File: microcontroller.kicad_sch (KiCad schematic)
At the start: 71 parts, among them J100 Conn_01x05_Pin, J101 Conn_01x03, J103 Screw_Terminal_01x02, J104 USB_C_Receptacle_USB2.0_16P, Q100 Si2371EDS, SW100 K2-1157SP-I4SW-04, U100 STM32H563RITx, U101 AP2112K-3.3, U102 USBLC6-2SC6, Y100 X322516MMB4SI

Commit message: Apply Daniel's suggestions
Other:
- moved on the sheet: FB100

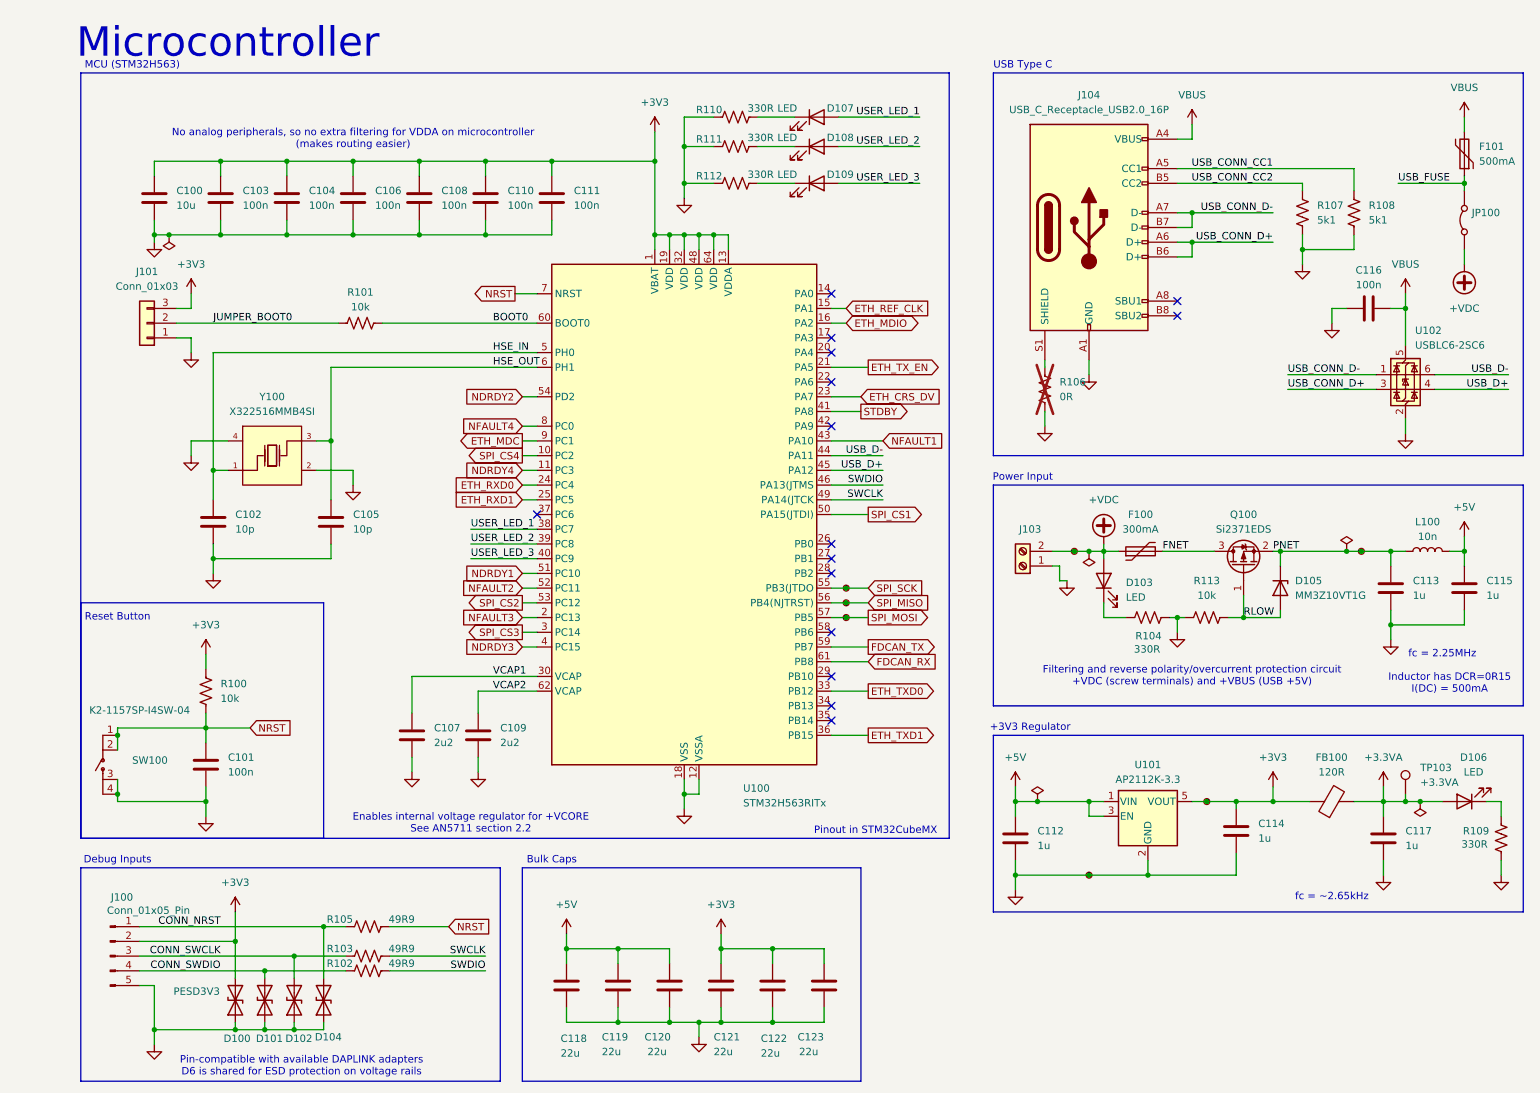
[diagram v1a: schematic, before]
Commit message: Modify repo for usage on Linux, add basic CI
chore: fix CI

Small things
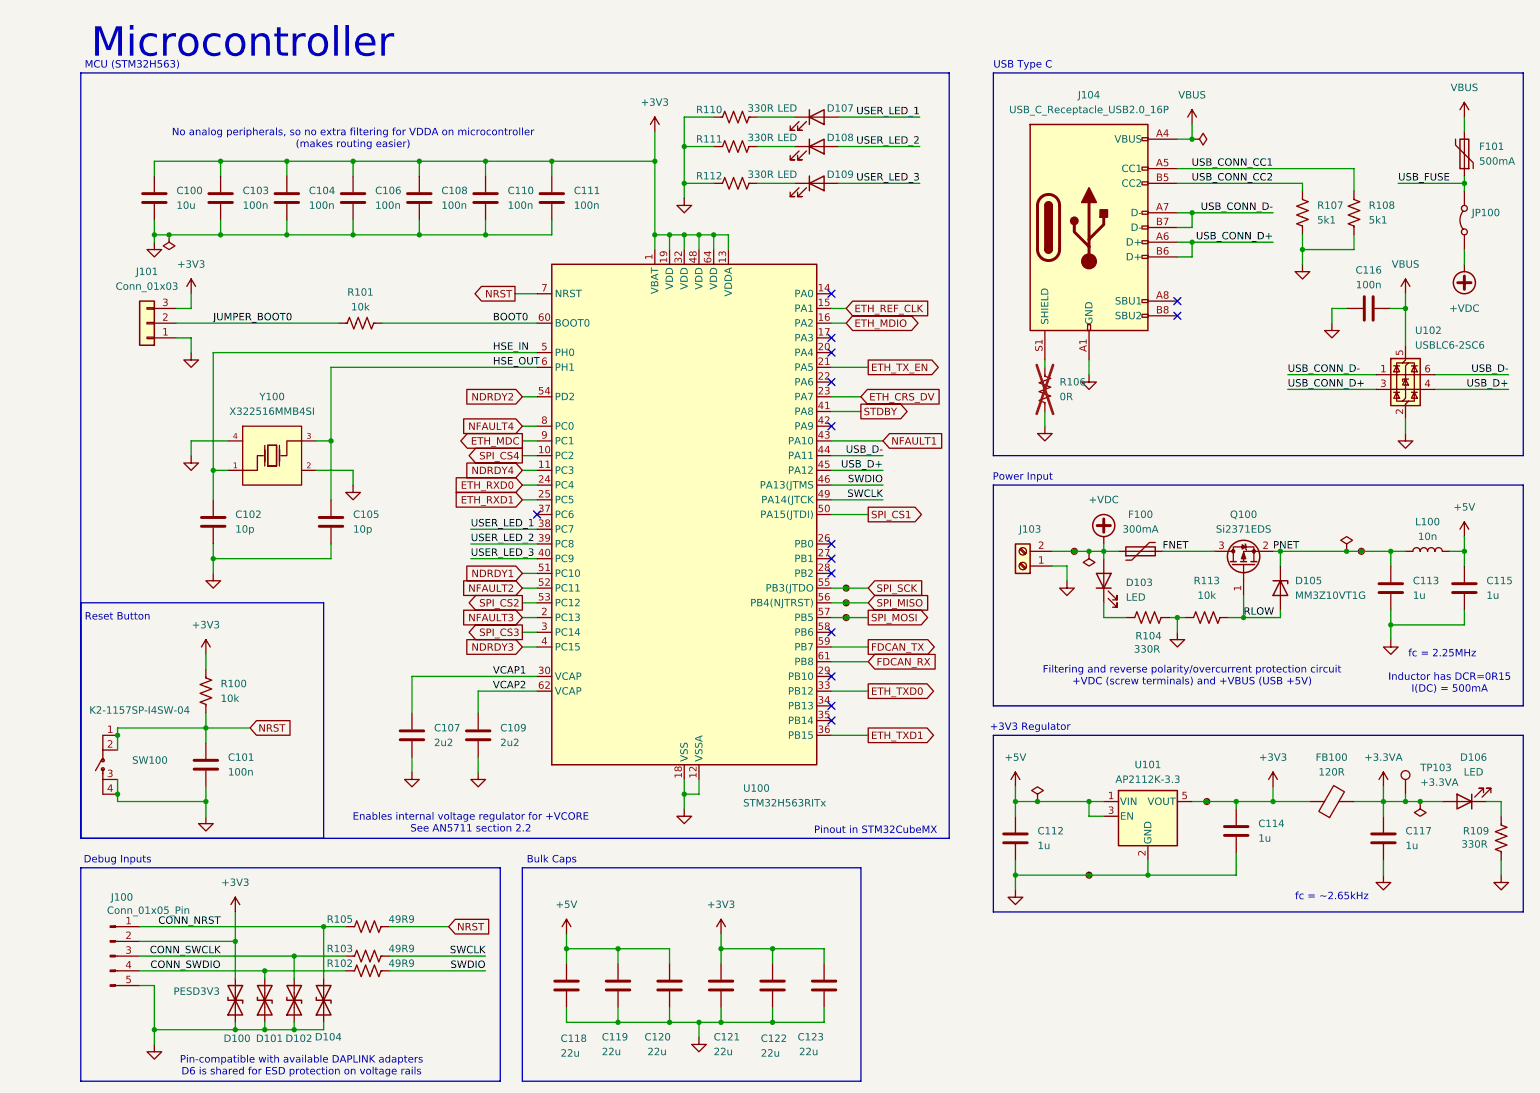
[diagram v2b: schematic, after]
